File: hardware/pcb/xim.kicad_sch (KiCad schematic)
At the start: 57 parts, among them IC1 RP2040_QFN56, SW1 RKB2, SW2 RKB2, U1 8MB QSPI, U2 RT9080-3.3, X2 USB A, X6 USB Type C, Y1 12MHz/12pF

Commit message: feat(hardware): add base schematic and USB-A load switch
- Strip battery charger, boost and Feather headers from the Adafruit import
- Add SY6280AAC load switch (1 A limit) from VBUS to the USB-A port
- Add custom xim symbol library
- Add no-connect flags and PWR_FLAGs; ERC clean
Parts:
- added C29: 1uF, Adafruit Feather RP2040 USB Host-import-fps:_0402NO, symbol Adafruit Feather RP2040 USB Host-eagle-import:CAP_CERAMIC_0402NO
- added R21: 6.8K, Adafruit Feather RP2040 USB Host-import-fps:_0402NO, symbol Adafruit Feather RP2040 USB Host-eagle-import:RESISTOR_0402NO
- added U3: SY6280AAC, Package_TO_SOT_SMD:SOT-23-5, symbol xim:SY6280AAC
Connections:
- net 5.0V: now also U3.1 (OUT)
- net 5V_EN: now also U3.4 (EN)
- net GND: now also C29.1, R21.2, U3.2 (GND)
- net VBUS: now also C29.2, U3.5 (IN)
- new net: R21.1, U3.3 (ISET)

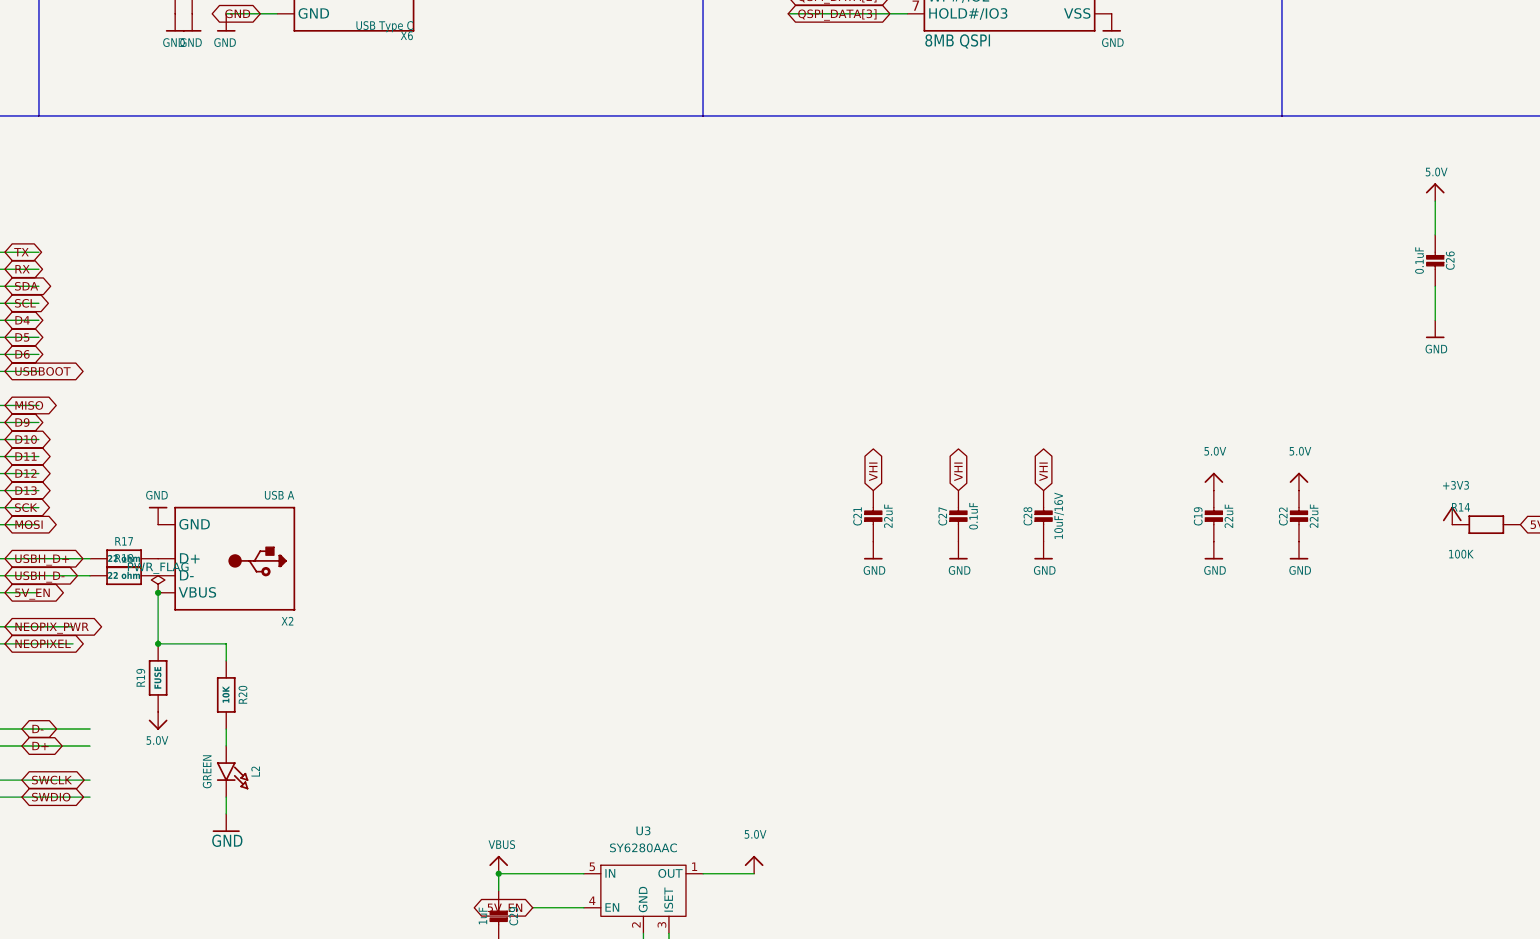
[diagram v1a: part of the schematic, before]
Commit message: feat(hardware): add FE1.1s USB hub with 2x USB-A and 1x USB-C host ports
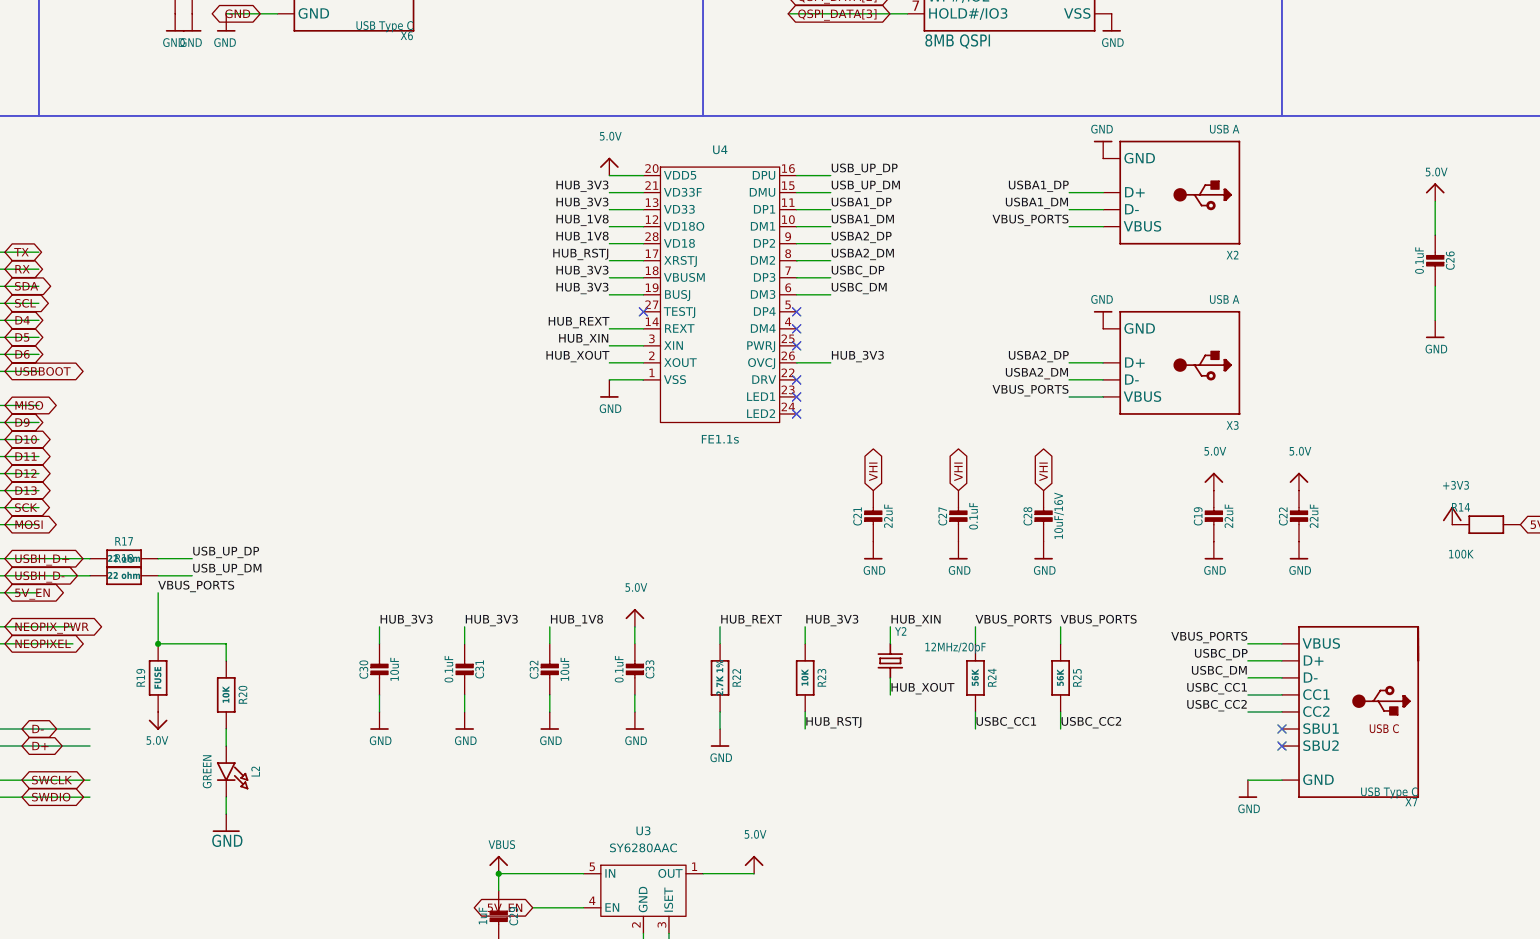
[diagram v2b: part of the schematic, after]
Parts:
- added C30, C32: 10uF, Adafruit Feather RP2040 USB Host-import-fps:0805-NO, symbol Adafruit Feather RP2040 USB Host-eagle-import:CAP_CERAMIC0805-NOOUTLINE
- added C31, C33: 0.1uF, Adafruit Feather RP2040 USB Host-import-fps:_0402NO, symbol Adafruit Feather RP2040 USB Host-eagle-import:CAP_CERAMIC_0402NO
- added R22: 2.7K 1%, Adafruit Feather RP2040 USB Host-import-fps:_0402NO, symbol Adafruit Feather RP2040 USB Host-eagle-import:RESISTOR_0402NO
- added R23: 10K, Adafruit Feather RP2040 USB Host-import-fps:_0402NO, symbol Adafruit Feather RP2040 USB Host-eagle-import:RESISTOR_0402NO
- added R24, R25: 56K, Adafruit Feather RP2040 USB Host-import-fps:_0402NO, symbol Adafruit Feather RP2040 USB Host-eagle-import:RESISTOR_0402NO
- added U4: FE1.1s, Package_SO:SSOP-28_3.9x9.9mm_P0.635mm, symbol xim:FE1.1s
- added X3: USB A, Adafruit Feather RP2040 USB Host-import-fps:USB_HOST-SMT, symbol Adafruit Feather RP2040 USB Host-eagle-import:USB_TYPEA_SMT
- added X7: USB Type C, Adafruit Feather RP2040 USB Host-import-fps:USB_C_CUSB31-CFM2AX-01-X, symbol Adafruit Feather RP2040 USB Host-eagle-import:USB_C
- added Y2: 12MHz/20pF, Adafruit Feather RP2040 USB Host-import-fps:CRYSTAL_2.5X2, symbol Adafruit Feather RP2040 USB Host-eagle-import:CRYSTAL2.5X2.0
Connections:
- net 5.0V: now also C33.2, U4.20 (VDD5)
- net GND: now also C30.2, C31.1, C32.2, C33.1, R22.2, U4.1 (VSS), X3.GND, X7.A1B12 (GND), X7.B1A12 (GND)
- net VBUS_PORTS: now reaches R19.1, R20.1, X2.VBUS
- net VBUS_PORTS: now also R24.1, R25.1, X3.VBUS, X7.A4B9 (VBUS), X7.B4A9 (VBUS)
- net USBA1_DP: now reaches X2.D+
- net USBA1_DP: now also U4.11 (DP1); no longer R17.1
- net USBA1_DM: now reaches X2.D-
- net USBA1_DM: now also U4.10 (DM1); no longer R18.1
- new net HUB_1V8: C32.1, U4.12 (VD18O), U4.28 (VD18)
- new net HUB_3V3: C30.1, C31.2, R23.1, U4.13 (VD33), U4.18 (VBUSM), U4.19 (BUSJ), U4.21 (VD33F), U4.26 (OVCJ)
- new net HUB_REXT: R22.1, U4.14 (REXT)
- new net HUB_RSTJ: R23.2, U4.17 (XRSTJ)
- new net HUB_XIN: U4.3 (XIN), Y2.3 (2)
- new net HUB_XOUT: U4.2 (XOUT), Y2.1
- new net USBA2_DM: U4.8 (DM2), X3.D-
- new net USBA2_DP: U4.9 (DP2), X3.D+
- new net USBC_CC1: R24.2, X7.A5 (CC1)
- new net USBC_CC2: R25.2, X7.B5 (CC2)
- new net USBC_DM: U4.6 (DM3), X7.A7 (D-), X7.B7 (D-)
- new net USBC_DP: U4.7 (DP3), X7.A6 (D+), X7.B6 (D+)
- new net USB_UP_DM: R18.1, U4.15 (DMU)
- new net USB_UP_DP: R17.1, U4.16 (DPU)
- no-connect marks 7 -> 16
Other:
- moved on the sheet: X2
